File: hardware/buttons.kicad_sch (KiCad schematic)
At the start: 27 parts, among them Q1 2N7002, Q2 2N7002, Q3 2N7002, Q4 2N7002, Q5 2N7002, Q6 2N7002

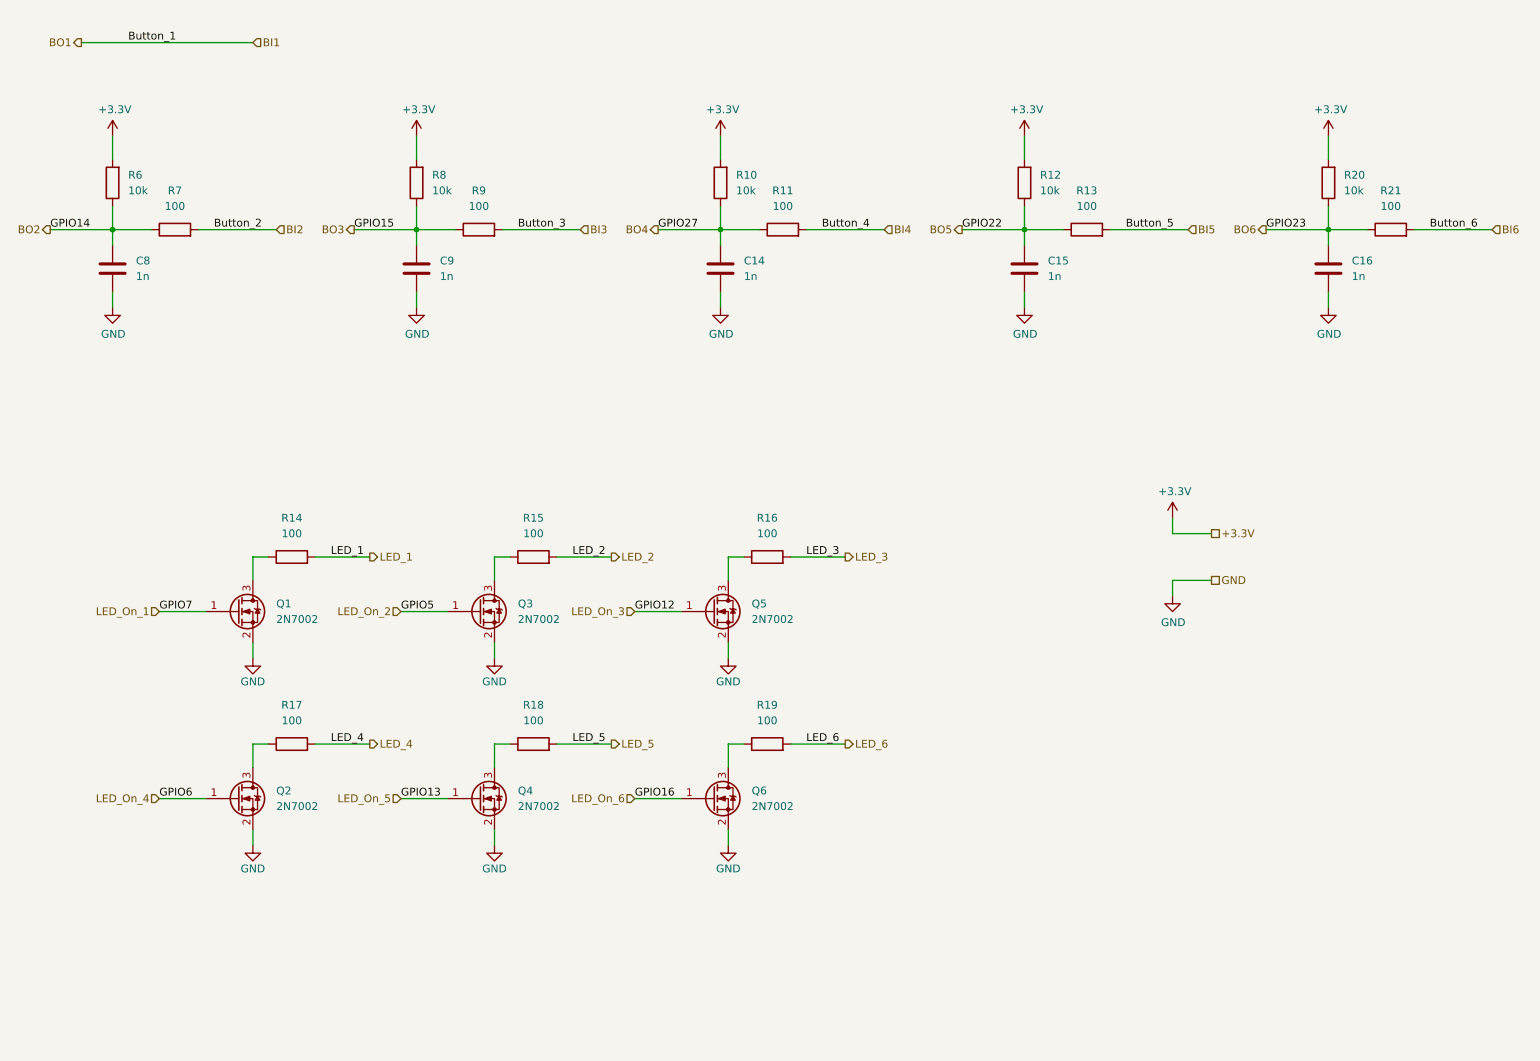
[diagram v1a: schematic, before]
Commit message: Add I2C header for displays. Mute/SHDN now controlled by previously unused GPIO20/26. LED1 is now hardwired to ON=V3P3 high. GPIO7 would still be available to control LED1. Change debounce circuit to have both directions up/down debounced. Use resistor/capacitor values to debounce button press times <100ms.
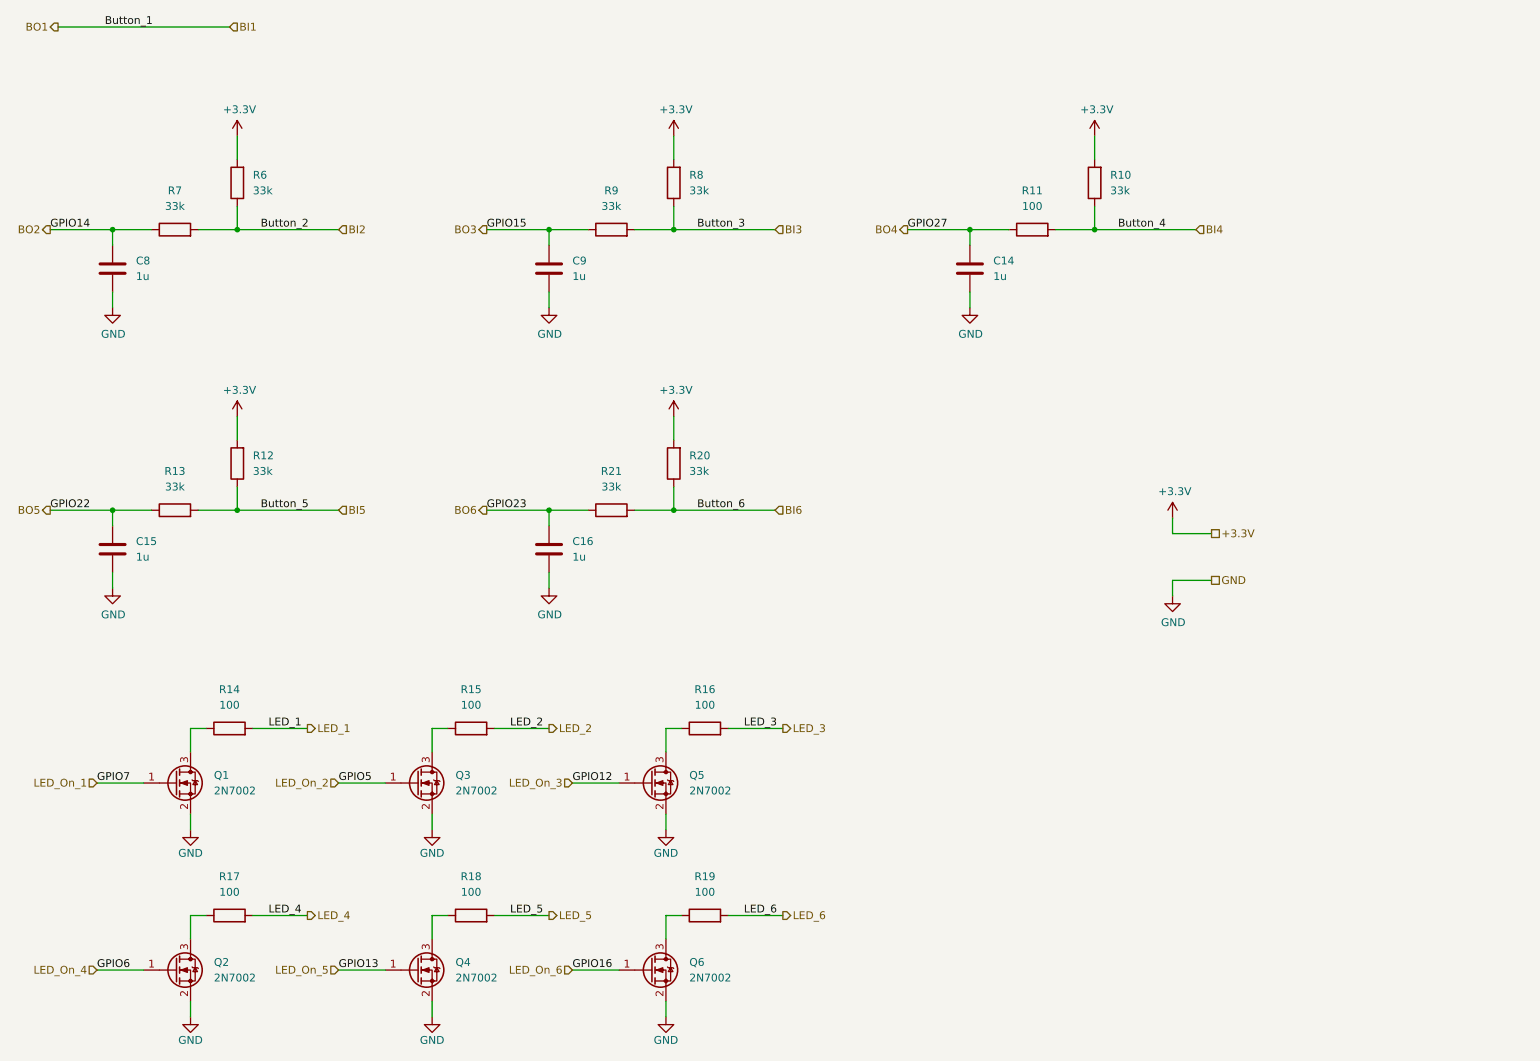
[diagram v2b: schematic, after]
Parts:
- C14, C15, C16, C8, C9: value 1n -> 1u
- R10, R12, R20, R6, R8: value 10k -> 33k
- R13, R21, R7, R9: value 100 -> 33k
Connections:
- net BI2: now also R6.1
- net BI3: now also R8.1
- net BI4: now also R10.1
- net BI5: now also R12.1
- net BI6: now also R20.1
- net BO2: no longer R6.1
- net BO3: no longer R8.1
- net BO4: no longer R10.1
- net BO5: no longer R12.1
- net BO6: no longer R20.1
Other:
- moved on the sheet: C14, C15, C16, C9, Q1, Q2, Q3, Q4, Q5, Q6, R10, R11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

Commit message: Add BOM descriptions and JLC PCB LCSC part numbers. Generate gerber, drill and pick-and-place files.
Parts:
- C14, C15, C16, C8, C9: Comment (none) -> X7R 16V; LCSC (none) -> EMK107B7105KA-T
- Q1, Q2, Q3, Q4, Q5, Q6: Comment (none) -> 60V; LCSC (none) -> C350313
- R10, R11, R12, R13, R14, R15, R16, R17, R18, R19, R20, R21, R6, R7, R8, R9: Comment (none) -> 5% 100ppm
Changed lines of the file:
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@@
+      (effects (font (size 1.27 1.27)) hide)
+    )
+    (property "Comment" "5% 100ppm" (id 4) (at 57.15 96.52 0)
       (effects (font (size 1.27 1.27)) hide)
     )
@@
       (effects (font (size 1.27 1.27)) hide)
     )
+    (property "Comment" "5% 100ppm" (id 4) (at 46.99 104.14 0)
+      (effects (font (size 1.27 1.27)) hide)
+    )
     (pin "1")
     (pin "2")
@@
       (effects (font (size 1.27 1.27)) hide)
     )
+    (property "Comment" "5% 100ppm" (id 4) (at 133.35 139.7 0)
+      (effects (font (size 1.27 1.27)) hide)
+    )
     (pin "1")
     (pin "2")
@@
     )
     (property "Datasheet" "~" (id 3) (at 107.95 64.77 0)
+      (effects (font (size 1.27 1.27)) hide)
+    )
+    (property "Comment" "X7R 16V" (id 4) (at 107.95 64.77 0)
+      (effects (font (size 1.27 1.27)) hide)
+    )
+    (property "LCSC" "EMK107B7105KA-T" (id 5) (at 107.95 64.77 0)
       (effects (font (size 1.27 1.27)) hide)
     )
@@
     )
     (property "Datasheet" "~" (id 3) (at 128.27 96.52 0)
+      (effects (font (size 1.27 1.27)) hide)
+    )
+    (property "Comment" "5% 100ppm" (id 4) (at 128.27 96.52 0)
       (effects (font (size 1.27 1.27)) hide)
     )
@@
       (effects (font (size 1.27 1.27)) hide)
     )
+    (property "Comment" "5% 100ppm" (id 4) (at 95.25 170.18 0)
+      (effects (font (size 1.27 1.27)) hide)
+    )
     (pin "1")
     (pin "2")
@@
     (property "Datasheet" "https://www.onsemi.com/pub/Collateral/NDS7002A-D.PDF" (id 3) (at 124.46 179.07 0)
       (effects (font (size 1.27 1.27)) (justify left) hide)
+    )
+    (property "Comment" "60V" (id 4) (at 124.46 179.07 0)
+      (effects (font (size 1.27 1.27)) hide)
+    )
+    (property "LCSC" "C350313" (id 5) (at 124.46 179.07 0)
+      (effects (font (size 1.27 1.27)) hide)
     )
     (pin "1")
@@
       (effects (font (size 1.27 1.27)) hide)
     )
+    (property "Comment" "5% 100ppm" (id 4) (at 57.15 50.8 0)
+      (effects (font (size 1.27 1.27)) hide)
+    )
     (pin "1")
     (pin "2")
@@
       (effects (font (size 1.27 1.27)) hide)
     )
+    (property "Comment" "5% 100ppm" (id 4) (at 46.99 58.42 0)
+      (effects (font (size 1.27 1.27)) hide)
+    )
     (pin "1")
     (pin "2")
@@
       (effects (font (size 1.27 1.27)) (justify left) hide)
     )
+    (property "Comment" "60V" (id 4) (at 86.36 179.07 0)
+      (effects (font (size 1.27 1.27)) hide)
+    )
+    (property "LCSC" "C350313" (id 5) (at 86.36 179.07 0)
+      (effects (font (size 1.27 1.27)) hide)
+    )
     (pin "1")
     (pin "2")
@@
       (effects (font (size 1.27 1.27)) hide)
     )
+    (property "Comment" "5% 100ppm" (id 4) (at 95.25 139.7 0)
+      (effects (font (size 1.27 1.27)) hide)
+    )
     (pin "1")
     (pin "2")
@@
       (effects (font (size 1.27 1.27)) hide)
     )
+    (property "Comment" "5% 100ppm" (id 4) (at 55.88 139.7 0)
+      (effects (font (size 1.27 1.27)) hide)
+    )
     (pin "1")
     (pin "2")
@@
       (effects (font (size 1.27 1.27)) hide)
     )
+    (property "Comment" "5% 100ppm" (id 4) (at 128.27 50.8 0)
+      (effects (font (size 1.27 1.27)) hide)
+    )
     (pin "1")
     (pin "2")
@@
       (effects (font (size 1.27 1.27)) hide)
     )
+    (property "Comment" "5% 100ppm" (id 4) (at 196.85 50.8 0)
+      (effects (font (size 1.27 1.27)) hide)
+    )
     (pin "1")
     (pin "2")
@@
       (effects (font (size 1.27 1.27)) hide)
     )
+    (property "Comment" "X7R 16V" (id 4) (at 36.83 64.77 0)
+      (effects (font (size 1.27 1.27)) hide)
+    )
+    (property "LCSC" "EMK107B7105KA-T" (id 5) (at 36.83 64.77 0)
+      (effects (font (size 1.27 1.27)) hide)
+    )
     (pin "1")
     (pin "2")
@@
     )
     (property "Datasheet" "~" (id 3) (at 36.83 110.49 0)
+      (effects (font (size 1.27 1.27)) hide)
+    )
+    (property "Comment" "X7R 16V" (id 4) (at 36.83 110.49 0)
+      (effects (font (size 1.27 1.27)) hide)
+    )
+    (property "LCSC" "EMK107B7105KA-T" (id 5) (at 36.83 110.49 0)
       (effects (font (size 1.27 1.27)) hide)
     )
@@
       (effects (font (size 1.27 1.27)) hide)
     )
+    (property "Comment" "5% 100ppm" (id 4) (at 55.88 170.18 0)
+      (effects (font (size 1.27 1.27)) hide)
+    )
     (pin "1")
     (pin "2")
@@
       (effects (font (size 1.27 1.27)) (justify left) hide)
     )
+    (property "Comment" "60V" (id 4) (at 46.99 148.59 0)
+      (effects (font (size 1.27 1.27)) hide)
+    )
+    (property "LCSC" "C350313" (id 5) (at 46.99 148.59 0)
+      (effects (font (size 1.27 1.27)) hide)
+    )
     (pin "1")
     (pin "2")
@@
       (effects (font (size 1.27 1.27)) hide)
     )
+    (property "Comment" "X7R 16V" (id 4) (at 107.95 110.49 0)
+      (effects (font (size 1.27 1.27)) hide)
+    )
+    (property "LCSC" "EMK107B7105KA-T" (id 5) (at 107.95 110.49 0)
+      (effects (font (size 1.27 1.27)) hide)
+    )
     (pin "1")
     (pin "2")
@@
     (property "Datasheet" "https://www.onsemi.com/pub/Collateral/NDS7002A-D.PDF" (id 3) (at 124.46 148.59 0)
       (effects (font (size 1.27 1.27)) (justify left) hide)
+    )
+    (property "Comment" "60V" (id 4) (at 124.46 148.59 0)
+      (effects (font (size 1.27 1.27)) hide)
+    )
+    (property "LCSC" "C350313" (id 5) (at 124.46 148.59 0)
+      (effects (font (size 1.27 1.27)) hide)
     )
     (pin "1")
@@
       (effects (font (size 1.27 1.27)) hide)
     )
+    (property "Comment" "5% 100ppm" (id 4) (at 133.35 170.18 0)
+      (effects (font (size 1.27 1.27)) hide)
+    )
     (pin "1")
     (pin "2")
@@
       (effects (font (size 1.27 1.27)) hide)
     )
+    (property "Comment" "5% 100ppm" (id 4) (at 118.11 104.14 0)
+      (effects (font (size 1.27 1.27)) hide)
+    )
     (pin "1")
     (pin "2")
@@
     )
     (property "Datasheet" "~" (id 3) (at 176.53 64.77 0)
+      (effects (font (size 1.27 1.27)) hide)
+    )
+    (property "Comment" "X7R 16V" (id 4) (at 176.53 64.77 0)
+      (effects (font (size 1.27 1.27)) hide)
+    )
+    (property "LCSC" "EMK107B7105KA-T" (id 5) (at 176.53 64.77 0)
       (effects (font (size 1.27 1.27)) hide)
     )
@@
       (effects (font (size 1.27 1.27)) hide)
     )
+    (property "Comment" "5% 100ppm" (id 4) (at 118.11 58.42 0)
+      (effects (font (size 1.27 1.27)) hide)
+    )
     (pin "1")
     (pin "2")
@@
     (property "Datasheet" "https://www.onsemi.com/pub/Collateral/NDS7002A-D.PDF" (id 3) (at 86.36 148.59 0)
       (effects (font (size 1.27 1.27)) (justify left) hide)
+    )
+    (property "Comment" "60V" (id 4) (at 86.36 148.59 0)
+      (effects (font (size 1.27 1.27)) hide)
+    )
+    (property "LCSC" "C350313" (id 5) (at 86.36 148.59 0)
+      (effects (font (size 1.27 1.27)) hide)
     )
     (pin "1")
@@
       (effects (font (size 1.27 1.27)) hide)
     )
+    (property "Comment" "5% 100ppm" (id 4) (at 186.69 58.42 0)
+      (effects (font (size 1.27 1.27)) hide)
+    )
     (pin "1")
     (pin "2")
@@
       (effects (font (size 1.27 1.27)) (justify left) hide)
     )
-    (pin "1")
+    (property "Comment" "60V" (id 4) (at 46.99 179.07 0)
+      (effects (font (size 1.27 1.27)) hide)
+    )
+    (property "LCSC" "C350313" (id 5) (at 46.99 179.07 0)
+      (effects (font (size 1.27 1.27)) hide)
+    )
+    (pin "1")
